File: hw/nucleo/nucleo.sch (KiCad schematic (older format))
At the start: 26 parts, among them J1 Rain, J2 Wind, J3 GPS, J4 BMP280, J5 Power, J6 Light, J7 I2C1, J8 I2C2, U1 MIC550X, U2 NUCLEO_L476RG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

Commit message: Released nucleo weather breakout v0.1 to kicad
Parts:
- J1, J2: footprint Connector_PinHeader_2.54mm:PinHeader_1x06_P2.54mm_Vertical -> alvarop:RJ11
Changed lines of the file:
@@
 encoding utf-8
 Sheet 1 1
-Title ""
-Date ""
-Rev ""
-Comp ""
+Title "Nucleo Weather Breakout"
+Date "2018-10-04"
+Rev "0.1"
+Comp "@alvaroprieto"
 Comment1 ""
 Comment2 ""
@@
 F 0 "J1" H 1420 2117 50  0000 C CNN
 F 1 "Rain" H 1420 2026 50  0000 C CNN
-F 2 "Connector_PinHeader_2.54mm:PinHeader_1x06_P2.54mm_Vertical" H 1500 1700 50  0001 C CNN
+F 2 "alvarop:RJ11" H 1500 1700 50  0001 C CNN
 F 3 "~" H 1500 1700 50  0001 C CNN
 	1    1500 1700
@@
 F 0 "J2" H 1420 3567 50  0000 C CNN
 F 1 "Wind" H 1420 3476 50  0000 C CNN
-F 2 "Connector_PinHeader_2.54mm:PinHeader_1x06_P2.54mm_Vertical" H 1500 3150 50  0001 C CNN
+F 2 "alvarop:RJ11" H 1500 3150 50  0001 C CNN
 F 3 "~" H 1500 3150 50  0001 C CNN
 	1    1500 3150
@@
 Wire Wire Line
 	7700 7800 8100 7800
-Text Label 8100 7800 2    50   ~ 0
+Text Label 8100 7900 2    50   ~ 0
 WDIR
 Wire Wire Line
@@
 Wire Wire Line
 	7700 7900 8100 7900
-Text Label 8100 7900 2    50   ~ 0
+Text Label 8100 7800 2    50   ~ 0
 LIGHT
 Wire Wire Line
@@
 Text Label 4800 3800 0    50   ~ 0
 XB_nRST
-Wire Wire Line
-	6500 6500 6100 6500
-Text Label 6100 6500 0    50   ~ 0
+Text Label 8200 6500 2    50   ~ 0
 XB_nRST
 Wire Wire Line
@@
 Wire Wire Line
 	7700 6500 8200 6500
-Text Label 8200 6500 2    50   ~ 0
+Text Label 9600 6500 0    50   ~ 0
 XB_ON
 NoConn ~ 6500 6600
@@
 NoConn ~ 7700 6900
 NoConn ~ 10000 6400
-NoConn ~ 10000 6500
 NoConn ~ 10000 6600
 NoConn ~ 10000 6700
@@
 GPS_PPS
 $Comp
-L power:PWR_FLAG #FLG?
+L power:PWR_FLAG #FLG0101
 U 1 1 5BC7DA90
 P 7900 7200
-F 0 "#FLG?" H 7900 7275 50  0001 C CNN
+F 0 "#FLG0101" H 7900 7275 50  0001 C CNN
 F 1 "PWR_FLAG" H 7900 7374 50  0000 C CNN
 F 2 "" H 7900 7200 50  0001 C CNN
@@
 	7900 7200 7700 7200
 $Comp
-L power:PWR_FLAG #FLG?
+L power:PWR_FLAG #FLG0102
 U 1 1 5BC7DCAA
 P 6050 7300
-F 0 "#FLG?" H 6050 7375 50  0001 C CNN
+F 0 "#FLG0102" H 6050 7375 50  0001 C CNN
 F 1 "PWR_FLAG" H 6050 7474 50  0000 C CNN
 F 2 "" H 6050 7300 50  0001 C CNN
@@
 Wire Wire Line
 	6050 7300 5700 7300
+Wire Wire Line
+	10000 6500 9600 6500
+NoConn ~ 6500 6500
 $EndSCHEMATC

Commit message: Starting work on PCB updates
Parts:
- removed J1: Rain, alvarop:RJ11, symbol Connector_Generic:Conn_01x06
- removed J2: Wind, alvarop:RJ11, symbol Connector_Generic:Conn_01x06
- removed J3: GPS, Connector_PinHeader_2.54mm:PinHeader_1x06_P2.54mm_Vertical, symbol Connector_Generic:Conn_01x06
- removed J4: BMP280, Connector_PinHeader_2.54mm:PinHeader_1x07_P2.54mm_Vertical, symbol Connector_Generic:Conn_01x07
- removed J8: I2C2, Connector_PinHeader_2.54mm:PinHeader_1x04_P2.54mm_Vertical, symbol Connector_Generic:Conn_01x04
- added ANT1: SR4G008, alvarop:SR4G008, symbol alvarop:SR4G008
- added C10, C12, C14: 1nF, Capacitor_SMD:C_0603_1608Metric, symbol Device:C_Small
- added C11, C13, C15, C6, C8: 22pF, Capacitor_SMD:C_0603_1608Metric, symbol Device:C_Small
- added C16: 0.1uF, Capacitor_SMD:C_0603_1608Metric, symbol Device:C_Small
- added C7: 2.2uF, Capacitor_SMD:C_0603_1608Metric, symbol Device:C_Small
- added C9: 22pF, Capacitor_SMD:C_0402_1005Metric, symbol Device:C_Small
- added J1: windrain, alvarop:043814-6621, symbol Connector_Generic:Conn_01x12
- added J2: Conn_01x02, Connector_PinHeader_2.54mm:PinHeader_1x02_P2.54mm_Vertical, symbol Connector_Generic:Conn_01x02
- added L1, L2: 47nH, Inductor_SMD:L_0603_1608Metric, symbol Device:L_Small
- added L3, L4: DNP, Inductor_SMD:L_0402_1005Metric, symbol Device:L_Small
- added R11: 10k, Resistor_SMD:R_0603_1608Metric, symbol Device:R_Small
- added U4: M10578-A2, alvarop:M10578-A2, symbol alvarop:M10578-A2
- added U5: BMP280, alvarop:BMP280, symbol alvarop:BMP280
- J7: value I2C1 -> AM2315
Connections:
- net labels added: GPS_FIX, GPS_SBY, GPS_nRST, XB_nSBY
- wire segments 135 -> 196
- no-connect marks 72 -> 64
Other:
- note added: "7-bit I2C Addr: 0x5C"
- note added: "7-bit I2C Addr: 0x76"
- moved on the sheet: C1, C3, C4, J6, J7, R1, R10, R2, R3, R4, R5, R6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

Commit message: Layout pretty much done. Time to review!
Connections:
- net GPS_FIX: now also U2.75 (PA3); no longer U2.61 (PA8)
- net GPS_PPS: now also U2.35 (PC2); no longer U2.69 (PB3)
- net GPS_SBY: now also U2.38 (PC0); no longer U2.65 (PB4)
- net GPS_nRST: now also U2.37 (PC3); no longer U2.63 (PB10)
- net LIGHT: now also U2.32 (PA4); no longer U2.30 (PA1)
- net RAIN: now also U2.4 (PD2); no longer U2.37 (PC3)
- net SCL: now also U2.41 (PB8); no longer U2.68 (PB13)
- net SDA: now also U2.43 (PB9); no longer U2.66 (PB14)
- net WDIR: now also U2.30 (PA1); no longer U2.32 (PA4)
- net WSPEED: now also U2.3 (PC12); no longer U2.35 (PC2)
- net XB_ON: now also U2.39 (PC9); no longer U2.41 (PB8)
- net XB_nRST: now also U2.42 (PC6); no longer U2.4 (PD2)
- net XB_nSBY: now also U2.40 (PC8); no longer U2.3 (PC12)
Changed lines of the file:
@@
 NoConn ~ 10050 2650
 NoConn ~ 10050 2750
-NoConn ~ 12700 3150
-NoConn ~ 12700 3250
 NoConn ~ 10050 2050
 NoConn ~ 10050 2150
@@
 Wire Wire Line
 	11250 2850 11650 2850
-Text Label 11650 2950 2    50   ~ 0
+Text Label 11650 2850 2    50   ~ 0
 WDIR
 Wire Wire Line
-	10050 3150 9550 3150
-Wire Wire Line
-	10050 3250 9550 3250
-Text Label 9550 3150 0    50   ~ 0
+	10050 1550 9650 1550
+Wire Wire Line
+	11250 1550 11600 1550
+Text Label 9650 1550 0    50   ~ 0
 WSPEED
-Text Label 9550 3250 0    50   ~ 0
+Text Label 11600 1550 2    50   ~ 0
 RAIN
 Wire Wire Line
 	10050 1450 9650 1450
 Wire Wire Line
-	11250 1450 11750 1450
+	11250 1450 11600 1450
 Text Label 9650 1450 0    50   ~ 0
 XB_RX
-Text Label 11750 1450 2    50   ~ 0
+Text Label 11600 1450 2    50   ~ 0
 XB_TX
 Wire Wire Line
@@
 Wire Wire Line
 	11250 2950 11650 2950
-Text Label 11650 2850 2    50   ~ 0
+Text Label 11650 2950 2    50   ~ 0
 LIGHT
 Wire Wire Line
-	13700 2850 14300 2850
-Wire Wire Line
-	13700 2750 14300 2750
-Text Label 14300 2750 2    50   ~ 0
+	12700 1550 12300 1550
+Wire Wire Line
+	12700 1650 12300 1650
+Text Label 12300 1650 0    50   ~ 0
 SDA
-Text Label 14300 2850 2    50   ~ 0
+Text Label 12300 1550 0    50   ~ 0
 SCL
 Wire Wire Line
@@
 Text Label 10600 5350 0    50   ~ 0
 XB_nRST
-Text Label 11750 1550 2    50   ~ 0
+Text Label 14100 1550 2    50   ~ 0
 XB_nRST
 Wire Wire Line
@@
 XB_ON
 Wire Wire Line
-	11250 1550 11750 1550
-Text Label 12300 1550 0    50   ~ 0
-XB_ON
+	12700 1450 12300 1450
 NoConn ~ 10050 1650
 NoConn ~ 10050 1750
@@
 NoConn ~ 11250 2050
 NoConn ~ 11250 1950
-NoConn ~ 12700 1450
-NoConn ~ 12700 1650
 NoConn ~ 12700 1750
 NoConn ~ 12700 2050
@@
 NoConn ~ 12700 2250
 NoConn ~ 12700 2350
-NoConn ~ 12700 2850
 NoConn ~ 13700 3050
 NoConn ~ 13700 2950
@@
 NoConn ~ 13700 1750
 NoConn ~ 13700 1650
-NoConn ~ 13700 1550
-NoConn ~ 13700 1450
 NoConn ~ 11250 3150
-NoConn ~ 11250 3250
 NoConn ~ 11250 1650
 NoConn ~ 10050 2250
@@
 NoConn ~ 12800 4250
 Wire Wire Line
-	12700 2950 12300 2950
-Text Label 12300 2950 0    50   ~ 0
+	10050 3250 9650 3250
+Text Label 9650 3150 0    50   ~ 0
 GPS_PPS
 $Comp
@@
 Wire Wire Line
 	9600 2350 9250 2350
-Wire Wire Line
-	12700 1550 12300 1550
 $Comp
 L Device:C_Small C10
@@
 XB_nSBY
 Wire Wire Line
-	10050 1550 9650 1550
-Text Label 9650 1550 0    50   ~ 0
+	13700 1550 14100 1550
+Text Label 14100 1450 2    50   ~ 0
 XB_nSBY
 $Comp
@@
 Connection ~ 4900 1300
 Wire Wire Line
-	12300 2550 12700 2550
-Text Label 12300 2550 0    50   ~ 0
+	9650 3150 10050 3150
+Text Label 12300 3250 0    50   ~ 0
 GPS_FIX
+Wire Wire Line
+	11250 3250 11650 3250
+Wire Wire Line
+	12700 3250 12300 3250
+Text Label 9650 3250 0    50   ~ 0
+GPS_nRST
+Text Label 11650 3250 2    50   ~ 0
+GPS_SBY
 $Comp
 L alvarop:NUCLEO_L476RG U2
@@
 	1    0    0    -1
 $EndComp
-Wire Wire Line
-	12700 2650 12300 2650
-Wire Wire Line
-	12700 2750 12300 2750
-Text Label 12300 2650 0    50   ~ 0
-GPS_nRST
-Text Label 12300 2750 0    50   ~ 0
-GPS_SBY
+NoConn ~ 12700 2550
+NoConn ~ 12700 2650
+NoConn ~ 12700 2750
+NoConn ~ 12700 2850
+NoConn ~ 12700 2950
+NoConn ~ 12700 3150
+Wire Wire Line
+	13700 1450 14100 1450
+Text Label 12300 1450 0    50   ~ 0
+XB_ON
+NoConn ~ 13700 2750
+NoConn ~ 13700 2850
 $EndSCHEMATC

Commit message: Updated part numbers
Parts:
- ANT1: DKPN (none) -> 627-1063-1-ND; MPN (none) -> SR4G008
- C1, C2, C5: DKPN (none) -> 490-1536-1-ND; MPN (none) -> GRM188R61C105KA93D
- C10, C12, C14: value 1nF -> 0.01 uF; DKPN (none) -> 311-1085-1-ND; MPN (none) -> CC0603KRX7R9BB103
- C11, C13, C15, C6, C8: DKPN (none) -> 1276-2228-1-ND; MPN (none) -> CL10C220JB8NFNC
- C16: DKPN (none) -> 490-1532-1-ND; MPN (none) -> GRM188R71C104KA01D
- C3: DKPN (none) -> 1276-2350-1-ND; MPN (none) -> CL10C8R2DB8NNNC
- C4: DKPN (none) -> 490-3896-1-ND; MPN (none) -> GRM188R60J106ME47D
- C7: DKPN (none) -> 1276-1085-1-ND; MPN (none) -> CL10A225KP8NNNC
- C9: value 22pF -> 1.5pF; DKPN (none) -> 490-3087-1-ND‎; MPN (none) -> ‎GJM1555C1H1R5CB01D‎
- J1: DKPN (none) -> WM4232-ND; MPN (none) -> 0438146621
- L1, L2: DKPN (none) -> 712-1442-1-ND‎; MPN (none) -> ‎L-14C47NJV4T
- L3: value DNP -> 12nH; DKPN (none) -> 490-2624-1-ND‎; MPN (none) -> ‎LQG15HS12NJ02D‎
- R1, R2, R3, R4, R5, R6: DKPN (none) -> 311-1.00KHRCT-ND; MPN (none) -> RC0603FR-071KL
- R10, R11: DKPN (none) -> 311-10.0KHRCT-ND; MPN (none) -> RC0603FR-0710KL
- R7, R8, R9: DKPN (none) -> 311-4.7KGRCT-ND; MPN (none) -> RC0603JR-074K7L
- U1: DKPN (none) -> 576-4764-1-ND; MPN (none) -> MIC5504-3.3YM5-TR
- U2: DKPN (none) -> SAM1086-19-ND; MPN (none) -> CES-119-01-T-D
- U3: DKPN (none) -> 1528-1392-ND; MPN (none) -> 366
- U4: DKPN (none) -> 627-1073-1-ND; MPN (none) -> M10578-A2
- U5: DKPN (none) -> 828-1064-1-ND; MPN (none) -> BMP280

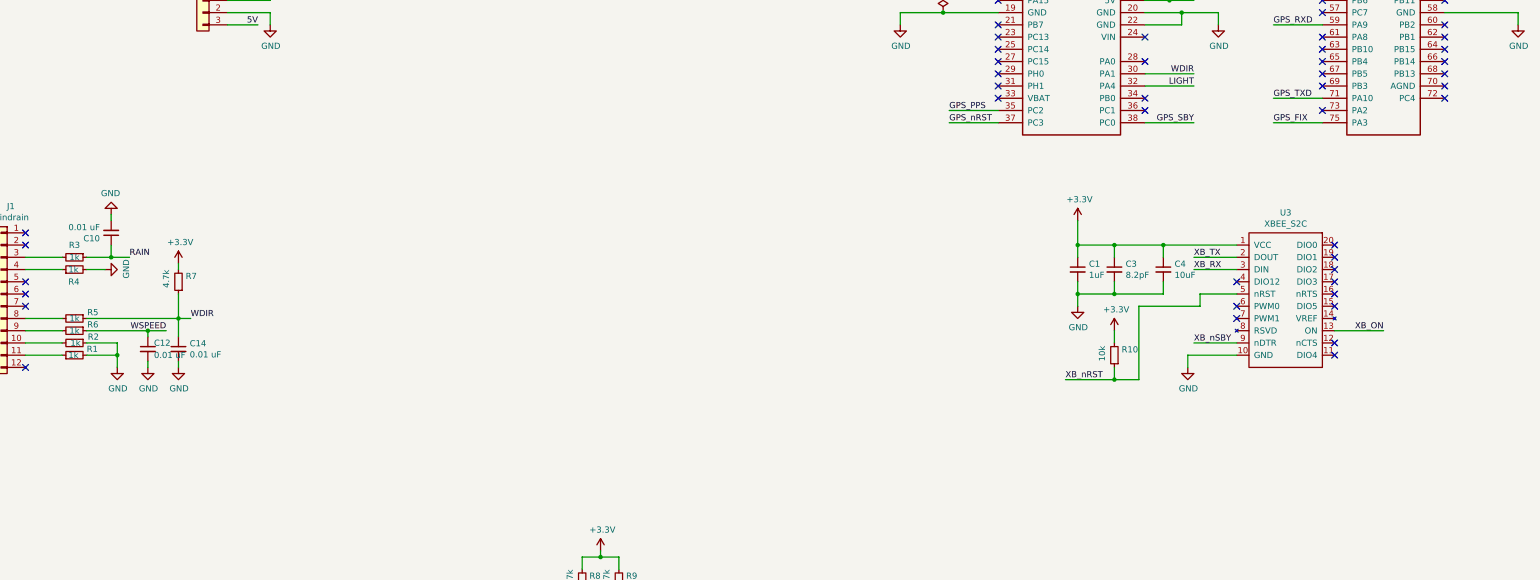
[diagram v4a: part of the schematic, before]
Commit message: Fixed wiring bugs from design
GPS_FIX line was shared with uart, so moved
WSPEED and WDIR pinout was flipped in new connector
RAIN unnaffected since it's just a reed switch
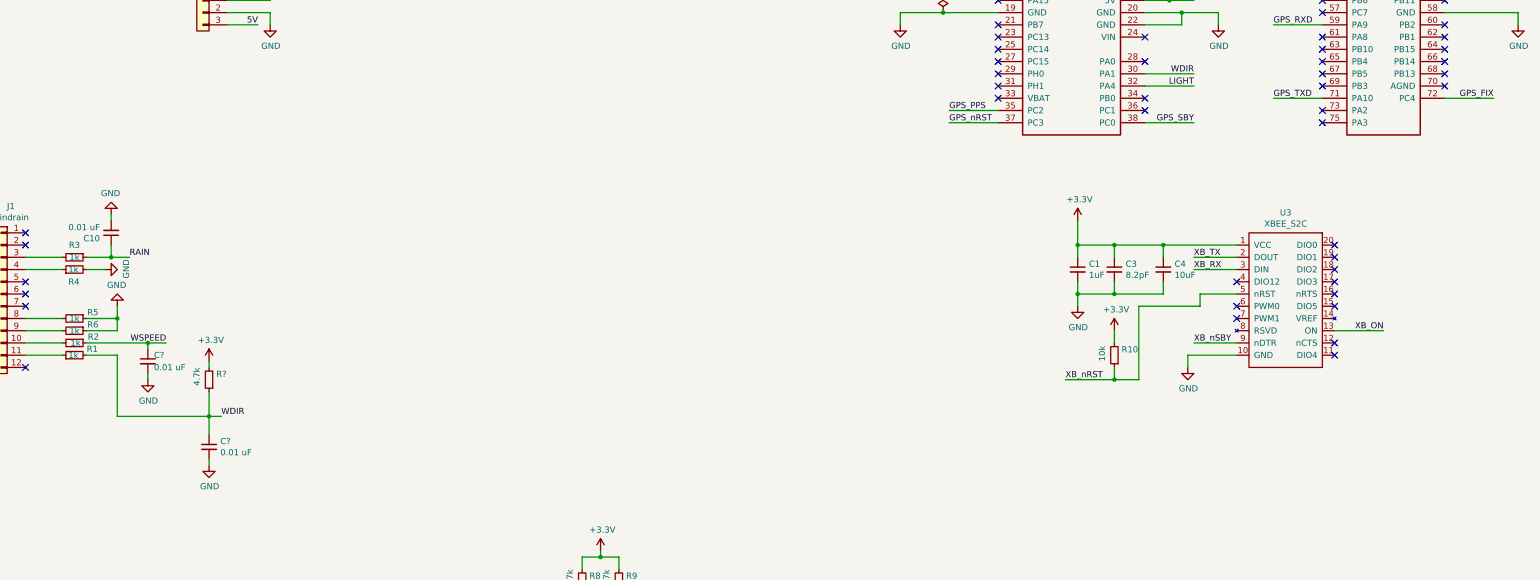
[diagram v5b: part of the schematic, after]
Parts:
- removed C12, C14: 0.01 uF, Capacitor_SMD:C_0603_1608Metric, symbol Device:C_Small
- removed R7: 4.7k, Resistor_SMD:R_0603_1608Metric, symbol Device:R_Small
- added C? (x2): 0.01 uF, Capacitor_SMD:C_0603_1608Metric, symbol Device:C_Small
- added R?: 4.7k, Resistor_SMD:R_0603_1608Metric, symbol Device:R_Small
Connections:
- net +3V3: now also R?.2
- net GND: now also R5.1, R6.1, C?.2, C?.2; no longer R1.2, R2.1
- net GPS_FIX: now also U2.72 (PC4); no longer U2.75 (PA3)
- net WDIR: now also R1.2, C?.1, R?.1; no longer R5.1
- net WSPEED: now also R2.1, C?.1; no longer R6.1
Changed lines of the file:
@@
 Sheet 1 1
 Title "Nucleo Weather Breakout"
-Date "2018-12-23"
-Rev "0.2"
+Date "2018-12-28"
+Rev "0.3"
 Comp "@alvaroprieto"
 Comment1 ""
@@
 	0    1    1    0
 $EndComp
-$Comp
-L Device:R_Small R7
-U 1 1 5BA9835C
-P 3350 4550
-F 0 "R7" H 3291 4504 50  0000 R CNN
-F 1 "4.7k" V 3450 4600 50  0000 R CNN
-F 2 "Resistor_SMD:R_0603_1608Metric" H 3350 4550 50  0001 C CNN
-F 3 "~" H 3350 4550 50  0001 C CNN
-F 4 "311-4.7KGRCT-ND" H 0   0   50  0001 C CNN "DKPN"
-F 5 " RC0603JR-074K7L" H 0   0   50  0001 C CNN "MPN"
-	1    3350 4550
-	-1   0    0    1
-$EndComp
 NoConn ~ 2100 4150
 NoConn ~ 2100 4250
@@
 	2100 4350 2400 4350
 Wire Wire Line
-	3350 4650 3350 4850
-Wire Wire Line
 	2400 4850 2100 4850
 Wire Wire Line
@@
 Wire Wire Line
 	2100 5050 2400 5050
-$Comp
-L power:GND #PWR01
-U 1 1 5BA98842
-P 2850 5250
-F 0 "#PWR01" H 2850 5000 50  0001 C CNN
-F 1 "GND" H 2855 5077 50  0000 C CNN
-F 2 "" H 2850 5250 50  0001 C CNN
-F 3 "" H 2850 5250 50  0001 C CNN
-	1    2850 5250
-	1    0    0    -1
-$EndComp
 $Comp
 L power:GND #PWR02
@@
 	0    -1   -1   0
 $EndComp
-Wire Wire Line
-	2600 4950 3100 4950
-$Comp
-L power:+3.3V #PWR07
-U 1 1 5BA98EC0
-P 3350 4400
-F 0 "#PWR07" H 3350 4250 50  0001 C CNN
-F 1 "+3.3V" H 3365 4573 50  0000 C CNN
-F 2 "" H 3350 4400 50  0001 C CNN
-F 3 "" H 3350 4400 50  0001 C CNN
-	1    3350 4400
-	1    0    0    -1
-$EndComp
-Wire Wire Line
-	3350 4400 3350 4450
 Text Label 2950 4350 0    50   ~ 0
 RAIN
-Text Label 3450 4850 0    50   ~ 0
-WDIR
-Text Label 3250 4950 2    50   ~ 0
-WSPEED
 $Comp
 L alvarop:MIC550X U1
@@
 NoConn ~ 12700 2250
 NoConn ~ 12700 2350
-NoConn ~ 13700 3050
+NoConn ~ 12700 3250
 NoConn ~ 13700 2950
 NoConn ~ 13700 2650
@@
 $EndComp
 $Comp
-L Device:C_Small C12
-U 1 1 5BE8D110
-P 3100 5100
-F 0 "C12" H 3150 5150 50  0000 L CNN
-F 1 "0.01 uF" H 3150 5050 50  0000 L CNN
-F 2 "Capacitor_SMD:C_0603_1608Metric" H 3100 5100 50  0001 C CNN
-F 3 "~" H 3100 5100 50  0001 C CNN
-F 4 "311-1085-1-ND" H 0   0   50  0001 C CNN "DKPN"
-F 5 "CC0603KRX7R9BB103" H 0   0   50  0001 C CNN "MPN"
-	1    3100 5100
-	1    0    0    -1
-$EndComp
-Wire Wire Line
-	3100 5200 3100 5250
-$Comp
-L power:GND #PWR0102
-U 1 1 5BE8D118
-P 3100 5250
-F 0 "#PWR0102" H 3100 5000 50  0001 C CNN
-F 1 "GND" H 3105 5077 50  0000 C CNN
-F 2 "" H 3100 5250 50  0001 C CNN
-F 3 "" H 3100 5250 50  0001 C CNN
-	1    3100 5250
-	1    0    0    -1
-$EndComp
-Wire Wire Line
-	3100 5000 3100 4950
-Connection ~ 3100 4950
-Wire Wire Line
-	3100 4950 3250 4950
-$Comp
-L Device:C_Small C14
-U 1 1 5BE9AEE1
-P 3350 5100
-F 0 "C14" H 3442 5146 50  0000 L CNN
-F 1 "0.01 uF" H 3442 5055 50  0000 L CNN
-F 2 "Capacitor_SMD:C_0603_1608Metric" H 3350 5100 50  0001 C CNN
-F 3 "~" H 3350 5100 50  0001 C CNN
-F 4 "311-1085-1-ND" H 0   0   50  0001 C CNN "DKPN"
-F 5 "CC0603KRX7R9BB103" H 0   0   50  0001 C CNN "MPN"
-	1    3350 5100
-	1    0    0    -1
-$EndComp
-Wire Wire Line
-	3350 5200 3350 5250
-$Comp
-L power:GND #PWR0103
-U 1 1 5BE9AEE9
-P 3350 5250
-F 0 "#PWR0103" H 3350 5000 50  0001 C CNN
-F 1 "GND" H 3355 5077 50  0000 C CNN
-F 2 "" H 3350 5250 50  0001 C CNN
-F 3 "" H 3350 5250 50  0001 C CNN
-	1    3350 5250
-	1    0    0    -1
-$EndComp
-Wire Wire Line
-	3350 5000 3350 4850
-Connection ~ 3350 4850
-Wire Wire Line
-	3350 4850 3450 4850
-$Comp
 L alvarop:XBEE_S2C U3
 U 1 1 5BABB5CF
@@
 $EndComp
 Wire Wire Line
-	2600 4850 3350 4850
-Wire Wire Line
 	2600 4350 2800 4350
 Wire Wire Line
@@
 Wire Wire Line
 	2100 5150 2400 5150
-Wire Wire Line
-	2600 5050 2850 5050
-Wire Wire Line
-	2850 5050 2850 5150
-Wire Wire Line
-	2600 5150 2850 5150
-Connection ~ 2850 5150
-Wire Wire Line
-	2850 5150 2850 5250
 $Comp
 L alvarop:M10578-A2 U4
@@
 Wire Wire Line
 	9650 3150 10050 3150
-Text Label 12300 3250 0    50   ~ 0
+Text Label 14100 3050 2    50   ~ 0
 GPS_FIX
 Wire Wire Line
 	11250 3250 11650 3250
 Wire Wire Line
-	12700 3250 12300 3250
+	13700 3050 14100 3050
 Text Label 9650 3250 0    50   ~ 0
 GPS_nRST
@@
 NoConn ~ 13700 2750
 NoConn ~ 13700 2850
+$Comp
+L power:GND #PWR?
+U 1 1 5C27B36D
+P 2850 4750
+F 0 "#PWR?" H 2850 4500 50  0001 C CNN
+F 1 "GND" H 2855 4577 50  0000 C CNN
+F 2 "" H 2850 4750 50  0001 C CNN
+F 3 "" H 2850 4750 50  0001 C CNN
+	1    2850 4750
+	-1   0    0    1
+$EndComp
+Wire Wire Line
+	2600 4850 2850 4850
+Wire Wire Line
+	2850 4850 2850 4950
+Wire Wire Line
+	2600 4950 2850 4950
+Wire Wire Line
+	2600 5050 3100 5050
+Text Label 3250 5050 2    50   ~ 0
+WSPEED
+$Comp
+L Device:C_Small C?
+U 1 1 5C290FD9
+P 3100 5200
+F 0 "C?" H 3150 5250 50  0000 L CNN
+F 1 "0.01 uF" H 3150 5150 50  0000 L CNN
+F 2 "Capacitor_SMD:C_0603_1608Metric" H 3100 5200 50  0001 C CNN
+F 3 "~" H 3100 5200 50  0001 C CNN
+F 4 "311-1085-1-ND" H 0   100 50  0001 C CNN "DKPN"
+F 5 "CC0603KRX7R9BB103" H 0   100 50  0001 C CNN "MPN"
+	1    3100 5200
+	1    0    0    -1
+$EndComp
+Wire Wire Line
+	3100 5300 3100 5350
+$Comp
+L power:GND #PWR?
+U 1 1 5C290FE1
+P 3100 5350
+F 0 "#PWR?" H 3100 5100 50  0001 C CNN
+F 1 "GND" H 3105 5177 50  0000 C CNN
+F 2 "" H 3100 5350 50  0001 C CNN
+F 3 "" H 3100 5350 50  0001 C CNN
+	1    3100 5350
+	1    0    0    -1
+$EndComp
+Wire Wire Line
+	3100 5100 3100 5050
+Connection ~ 3100 5050
+Wire Wire Line
+	3100 5050 3250 5050
+$Comp
+L Device:R_Small R?
+U 1 1 5C2B14C1
+P 3600 5350
+F 0 "R?" H 3541 5304 50  0000 R CNN
+F 1 "4.7k" V 3700 5400 50  0000 R CNN
+F 2 "Resistor_SMD:R_0603_1608Metric" H 3600 5350 50  0001 C CNN
+F 3 "~" H 3600 5350 50  0001 C CNN
+F 4 "311-4.7KGRCT-ND" H 250 800 50  0001 C CNN "DKPN"
+F 5 " RC0603JR-074K7L" H 250 800 50  0001 C CNN "MPN"
+	1    3600 5350
+	-1   0    0    1
+$EndComp
+Wire Wire Line
+	3600 5450 3600 5650
+$Comp
+L power:+3.3V #PWR?
+U 1 1 5C2B14C9
+P 3600 5200
+F 0 "#PWR?" H 3600 5050 50  0001 C CNN
+F 1 "+3.3V" H 3615 5373 50  0000 C CNN
+F 2 "" H 3600 5200 50  0001 C CNN
+F 3 "" H 3600 5200 50  0001 C CNN
+	1    3600 5200
+	1    0    0    -1
+$EndComp
+Wire Wire Line
+	3600 5200 3600 5250
+Text Label 3700 5650 0    50   ~ 0
+WDIR
+$Comp
+L Device:C_Small C?
+U 1 1 5C2B14D3
+P 3600 5900
+F 0 "C?" H 3692 5946 50  0000 L CNN
+F 1 "0.01 uF" H 3692 5855 50  0000 L CNN
+F 2 "Capacitor_SMD:C_0603_1608Metric" H 3600 5900 50  0001 C CNN
+F 3 "~" H 3600 5900 50  0001 C CNN
+F 4 "311-1085-1-ND" H 250 800 50  0001 C CNN "DKPN"
+F 5 "CC0603KRX7R9BB103" H 250 800 50  0001 C CNN "MPN"
+	1    3600 5900
+	1    0    0    -1
+$EndComp
+Wire Wire Line
+	3600 6000 3600 6050
+$Comp
+L power:GND #PWR?
+U 1 1 5C2B14DB
+P 3600 6050
+F 0 "#PWR?" H 3600 5800 50  0001 C CNN
+F 1 "GND" H 3605 5877 50  0000 C CNN
+F 2 "" H 3600 6050 50  0001 C CNN
+F 3 "" H 3600 6050 50  0001 C CNN
+	1    3600 6050
+	1    0    0    -1
+$EndComp
+Wire Wire Line
+	3600 5800 3600 5650
+Connection ~ 3600 5650
+Wire Wire Line
+	3600 5650 3700 5650
+Wire Wire Line
+	2850 5650 3600 5650
+Wire Wire Line
+	2850 5650 2850 5150
+Wire Wire Line
+	2850 5150 2600 5150
+Connection ~ 2850 4850
+Wire Wire Line
+	2850 4850 2850 4750
 $EndSCHEMATC
